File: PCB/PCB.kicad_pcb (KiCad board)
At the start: 2 copper layers, 100 x 120 mm, 17 parts, among them SW1 SW_Push, SW2 SW_Push, SW3 SW_Push, SW4 SW_Push, SW5 SW_Push, SW6 SW_Push, U1 NodeMCU_1.0_(ESP-12E)

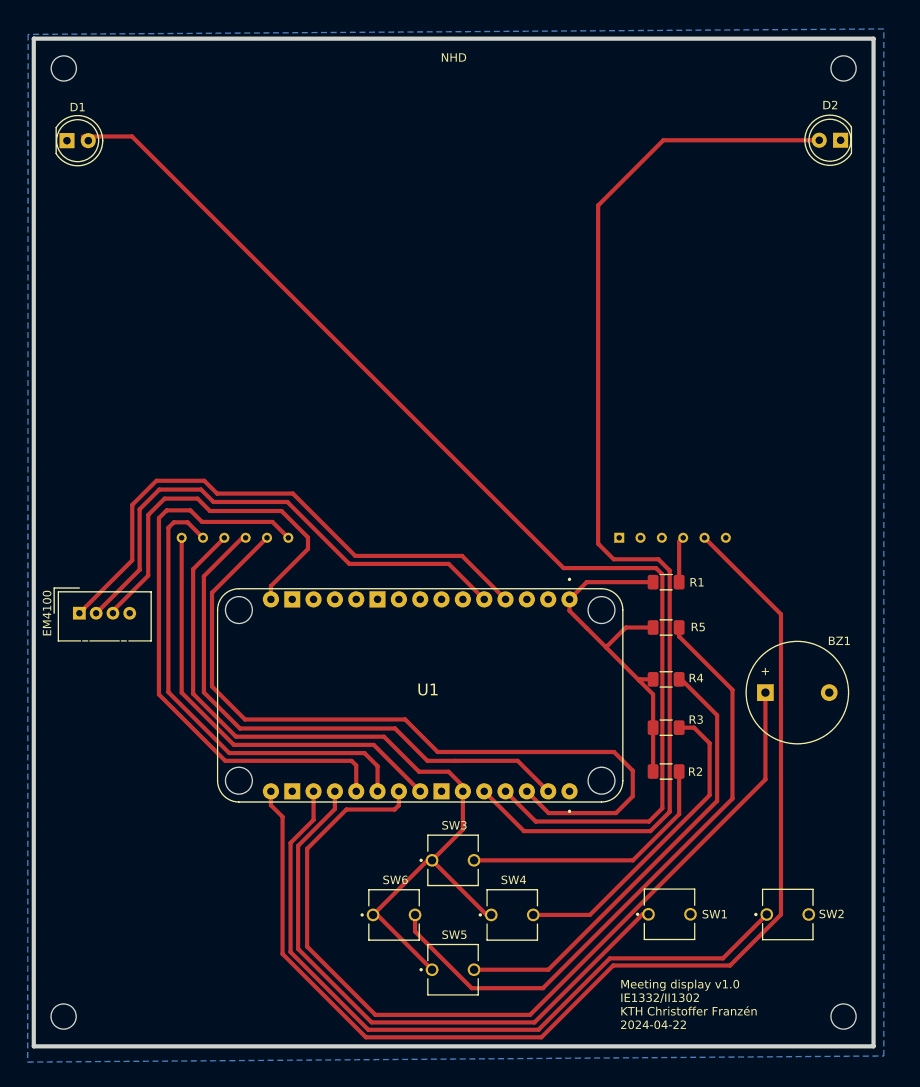
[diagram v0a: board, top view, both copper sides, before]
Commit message: drawn new PCB based on feedback
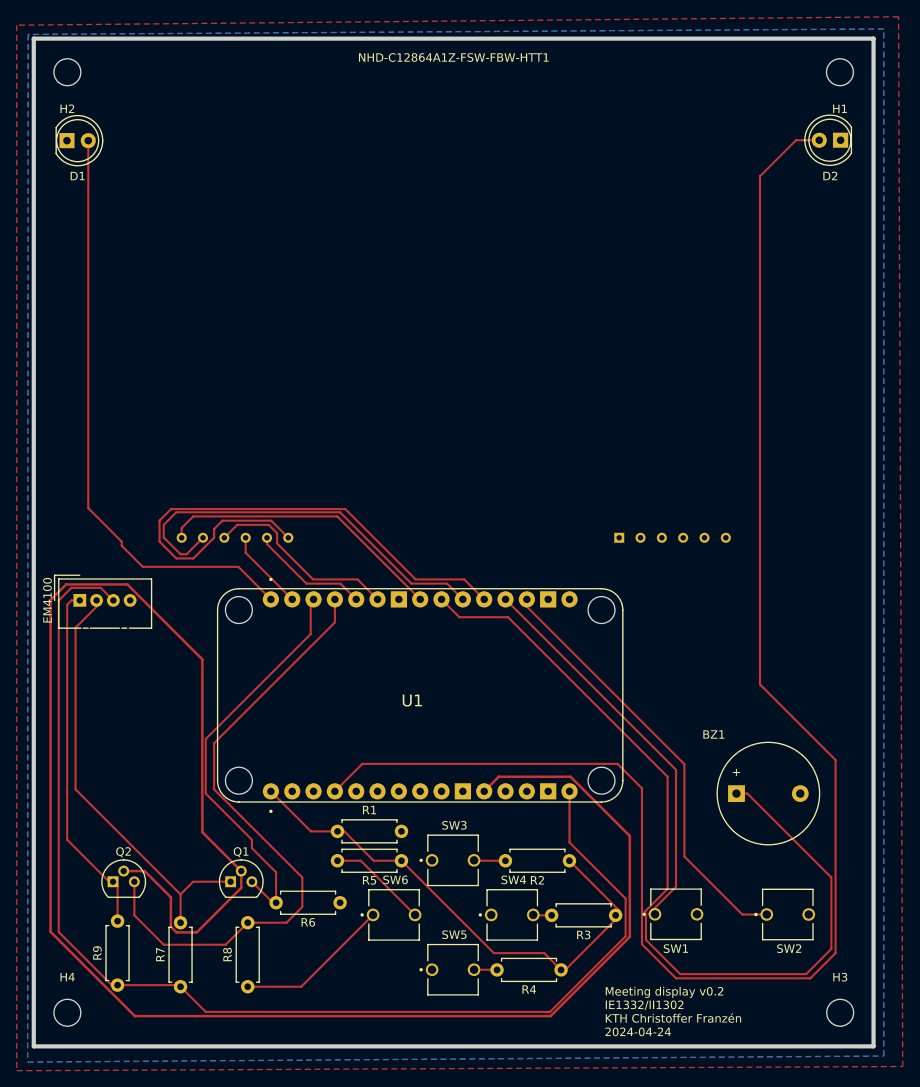
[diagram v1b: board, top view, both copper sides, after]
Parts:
- added H1: MountingHole_Pad, MountingHole:MountingHole_3.2mm_M3, F.Cu at (183.5, 30.1)
- added H2: MountingHole_Pad, MountingHole:MountingHole_3.2mm_M3, F.Cu at (91.5, 30.1)
- added H3: MountingHole_Pad, MountingHole:MountingHole_3.2mm_M3, F.Cu at (183.6, 142.1)
- added H4: MountingHole_Pad, MountingHole:MountingHole_3.2mm_M3, F.Cu at (91.5, 142.1)
- added Q1: NMOS, Package_TO_SOT_THT:TO-92, F.Cu at (111.0, 126.5)
- added Q2: NMOS, Package_TO_SOT_THT:TO-92, F.Cu at (97.0, 126.5)
- added R6: 10k, Resistor_THT:R_Axial_DIN0207_L6.3mm_D2.5mm_P7.62mm_Horizontal, F.Cu at (124.0, 129.0)
- added R7: 10k, Resistor_THT:R_Axial_DIN0207_L6.3mm_D2.5mm_P7.62mm_Horizontal, F.Cu at (105.0, 139.0)
- added R8: 10k, Resistor_THT:R_Axial_DIN0207_L6.3mm_D2.5mm_P7.62mm_Horizontal, F.Cu at (113.0, 139.0)
- added R9: 10k, Resistor_THT:R_Axial_DIN0207_L6.3mm_D2.5mm_P7.62mm_Horizontal, F.Cu at (97.5, 138.8)
- R1, R2, R3, R4, R5: footprint Resistor_SMD:R_1206_3216Metric_Pad1.30x1.75mm_HandSolder -> Resistor_THT:R_Axial_DIN0207_L6.3mm_D2.5mm_P7.62mm_Horizontal
- moved R1 43.3 mm to (131.3, 120.5)
- moved R5 42.0 mm to (131.3, 124.0), turned to 180 degrees
- moved R4 36.8 mm to (150.3, 137.0), turned to 180 degrees
- moved R3 23.1 mm to (156.8, 130.5), turned to 180 degrees
- moved R2 15.7 mm to (151.3, 124.0), turned to 180 degrees
- moved BZ1 12.5 mm to (171.2, 116.0)
- moved EM4100 1.53 mm to (93.0, 93.0)
- moved SW1 0.78 mm to (164.0, 130.4)
- turned U1 to 90 degrees
- renumbered NHD to NHD-C12864A1Z-FSW-FBW-HTT1
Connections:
- net /Analog buttons renamed BUTTONS
- net Net-(BZ1-+) renamed BUZZER
- net Net-(NHD-C12864A1Z-FSW-FBW-HTT1-A0) renamed A0
- net Net-(NHD-C12864A1Z-FSW-FBW-HTT1-SCL) renamed SCL
- net Net-(NHD-C12864A1Z-FSW-FBW-HTT1-SI) renamed SI
- net Net-(NHD-C12864A1Z-FSW-FBW-HTT1-~{CS}) renamed ~{CS}
- net Net-(U1-RX(DPIO3)) renamed SW1
- net Net-(U1-TX(GPIO1)) renamed SW2
- net VCC renamed +5V
- D1 pad 2: Net-(D1-A) -> RED
- D2 pad 2: Net-(D2-A) -> GREEN
- EM4100 pad 1: Net-(EM4100-TX) -> HV2
- EM4100 pad 2: Net-(EM4100-RX) -> HV1
- NHD-C12864A1Z-FSW-FBW-HTT1 pad 11: Net-(NHD-C12864A1Z-FSW-FBW-HTT1-LED+) -> +3.3V
- NHD-C12864A1Z-FSW-FBW-HTT1 pad 3: Net-(NHD-C12864A1Z-FSW-FBW-HTT1-VDD) -> +3.3V
- NHD-C12864A1Z-FSW-FBW-HTT1 pad 5: Net-(NHD-C12864A1Z-FSW-FBW-HTT1-~{RESET}) -> ~{RESET}
- SW3 pad 1: Net-(NHD-C12864A1Z-FSW-FBW-HTT1-VDD) -> +3.3V
- SW4 pad 1: Net-(NHD-C12864A1Z-FSW-FBW-HTT1-VDD) -> +3.3V
- SW5 pad 1: Net-(NHD-C12864A1Z-FSW-FBW-HTT1-VDD) -> +3.3V
- SW6 pad 1: Net-(NHD-C12864A1Z-FSW-FBW-HTT1-VDD) -> +3.3V
- U1 pad 11: unconnected-(U1-3.3V-Pad11) -> +3.3V
- U1 pad 16: Net-(NHD-C12864A1Z-FSW-FBW-HTT1-LED+) -> +3.3V
- U1 pad 25: Net-(NHD-C12864A1Z-FSW-FBW-HTT1-VDD) -> +3.3V
- U1 pad 26: Net-(D2-A) -> ~{RESET}
- U1 pad 27: Net-(D1-A) -> LV2
- U1 pad 28: Net-(NHD-C12864A1Z-FSW-FBW-HTT1-~{RESET}) -> LV1
- U1 pad 30: unconnected-(U1-D0(GPIO16)-Pad30) -> RED
- U1 pad 4: Net-(EM4100-TX) -> GREEN
- U1 pad 5: Net-(EM4100-RX) -> unconnected-(U1-SD2(GPIO9)-Pad5)
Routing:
- net +3.3V: track 0.00 -> 264.2 mm
- net GREEN: track 0.00 -> 188.7 mm
- net Net-(D1-A): track 139.3 -> 0.00 mm
- net Net-(NHD-C12864A1Z-FSW-FBW-HTT1-LED+): track 138.1 -> 0.00 mm
- net Net-(D2-A): track 133.4 -> 0.00 mm
- net +5V: track 44.4 -> 142.9 mm
- net Net-(NHD-C12864A1Z-FSW-FBW-HTT1-VDD): track 96.9 -> 0.00 mm
- net Net-(NHD-C12864A1Z-FSW-FBW-HTT1-~{RESET}): track 92.2 -> 0.00 mm
- net LV2: track 0.00 -> 74.2 mm
- net RED: track 0.00 -> 70.3 mm
- net Net-(EM4100-TX): track 67.0 -> 0.00 mm
- net Net-(R5-Pad2): track 74.9 -> 11.9 mm
- net Net-(EM4100-RX): track 61.9 -> 0.00 mm
- net A0: track 66.6 -> 9.63 mm
- net HV1: track 0.00 -> 51.2 mm
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- added copper zone on F.Cu, net +3.3V
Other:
- outline, holes or cut-outs redrawn
- board text added: "Meeting display v0.2 IE1332/II1302 KTH Christoffer Franzén 2024-04-24"
- board text removed: "Meeting display v1.0 IE1332/II1302 KTH Christoffer Franzén 2024-04-22"

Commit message: small fix
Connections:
- U1 pad 10: unconnected-(U1-GND-Pad10) -> GND
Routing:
- net LV2: track 74.2 -> 69.7 mm
- net LV1: track 48.8 -> 45.2 mm

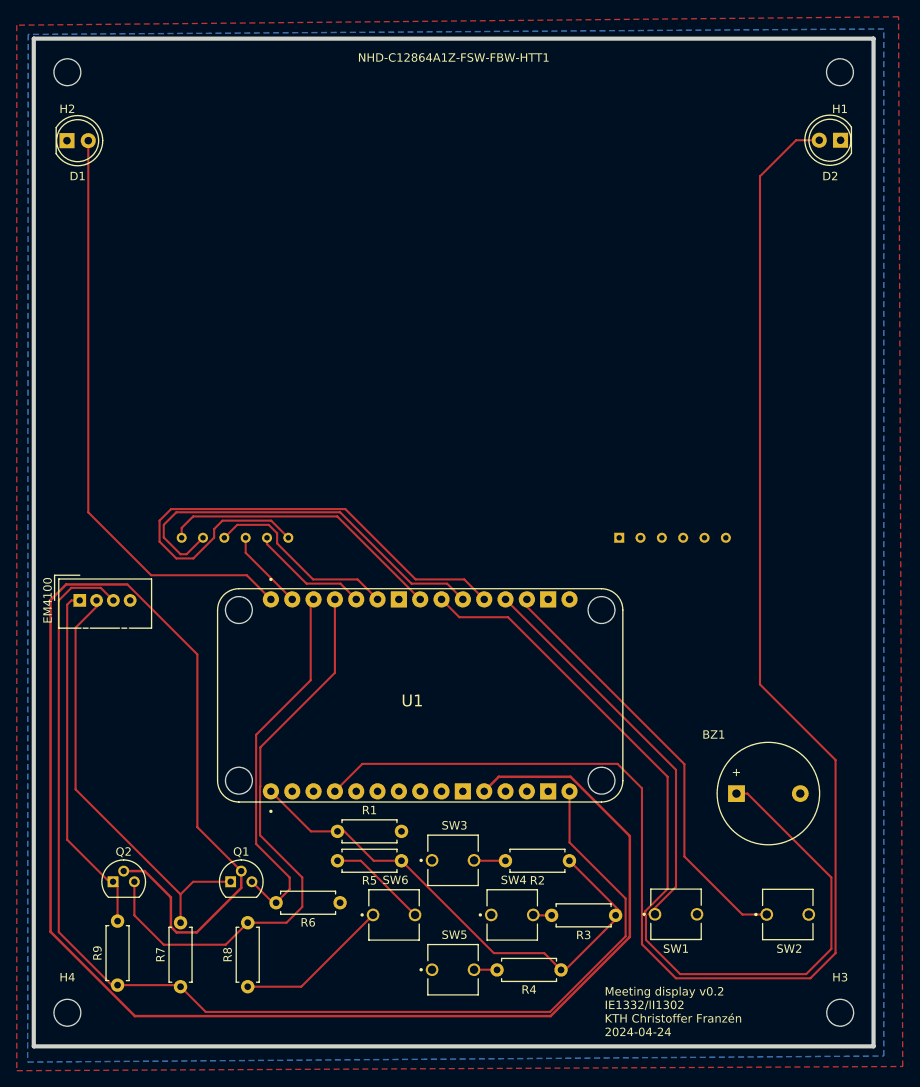
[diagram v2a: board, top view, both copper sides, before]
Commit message: Fixed all errors and drawn tracks on 2nd layer
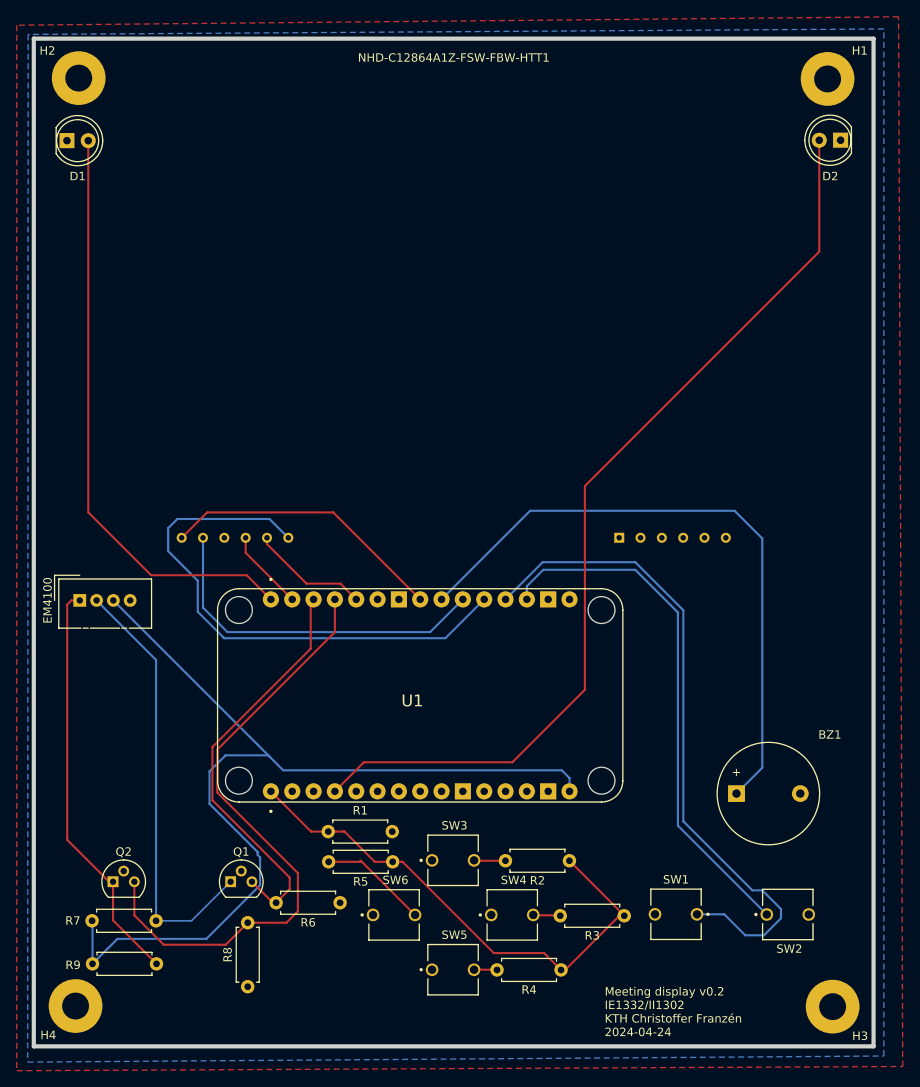
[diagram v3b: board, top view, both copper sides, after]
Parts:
- H1, H2, H3, H4: footprint MountingHole:MountingHole_3.2mm_M3 -> MountingHole:MountingHole_3.2mm_M3_Pad
- moved R7 13.1 mm to (94.5, 131.2), turned to 0 degrees
- moved R9 3.92 mm to (94.5, 136.3), turned to 0 degrees
- moved H1 1.68 mm to (182.1, 30.9)
- moved H2 1.52 mm to (92.9, 30.8)
- moved H4 1.26 mm to (92.5, 141.3)
- moved H3 1.16 mm to (182.7, 141.4)
- moved R1 1.10 mm to (130.2, 120.5)
- moved R5 1.06 mm to (130.3, 124.1)
- moved R3 1.03 mm to (157.8, 130.6)
- turned SW1 to 180 degrees
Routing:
- net +3.3V: track 264.2 -> 0.00 mm
- net GREEN: track 188.7 -> 111.8 mm
- net SW1: track 47.3 -> 79.4 mm
- net BUZZER: track 105.2 -> 75.6 mm
- net +5V: track 142.9 -> 117.9 mm
- net SW2: track 51.1 -> 62.8 mm
- net HV2: track 42.2 -> 49.9 mm
- net SI: track 48.4 -> 42.1 mm
- net LV1: track 45.2 -> 49.5 mm
- net LV2: track 69.7 -> 73.5 mm
- net ~{CS}: track 65.7 -> 64.5 mm
- net Net-(R5-Pad2): track 11.9 -> 13.0 mm
- net HV1: track 51.2 -> 52.0 mm

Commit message: inital final
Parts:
- moved Q1 1.63 mm to (109.3, 126.4)
- moved H2 0.21 mm to (92.7, 30.9)
- renumbered NHD-C12864A1Z-FSW-FBW-HTT1 to NHD
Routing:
- net LV1: track 49.5 -> 51.4 mm
- net RED: track 70.3 -> 69.5 mm
- net HV1: track 52.0 -> 51.3 mm
- net SW1: track 79.4 -> 78.7 mm
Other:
- board text added: "Meeting display v0.2 IE1332/II1302 KTH Christoffer Franzén 2024-04-25"
- board text removed: "Meeting display v0.2 IE1332/II1302 KTH Christoffer Franzén 2024-04-24"

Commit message: final
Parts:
- moved Q2 10.3 mm to (104.9, 133.0)
- moved R7 8.31 mm to (100.5, 136.8), turned to 90 degrees
- moved R9 8.31 mm to (100.6, 142.0)
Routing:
- net LV2: track 73.5 -> 59.7 mm
- net HV2: track 49.9 -> 62.8 mm
- net +5V: track 118.3 -> 114.4 mm
- net HV1: track 51.3 -> 49.3 mm
